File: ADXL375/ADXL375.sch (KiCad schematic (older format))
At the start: 23 parts, among them J1 Conn_01x06, J2 Conn_01x04, J3 Conn_01x06, J4 Conn_01x04, Q1 BSS138DW, Q2 BSS138DW, U1 AP2127K-3.3, U2 ADXL345

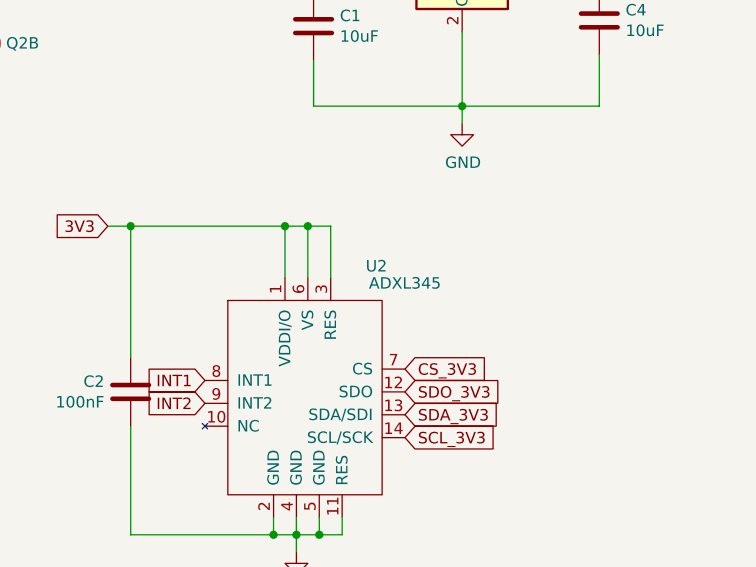
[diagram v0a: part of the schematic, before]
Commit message: ADXL375 Schematic Update
ADXL345 changed to ADXL375
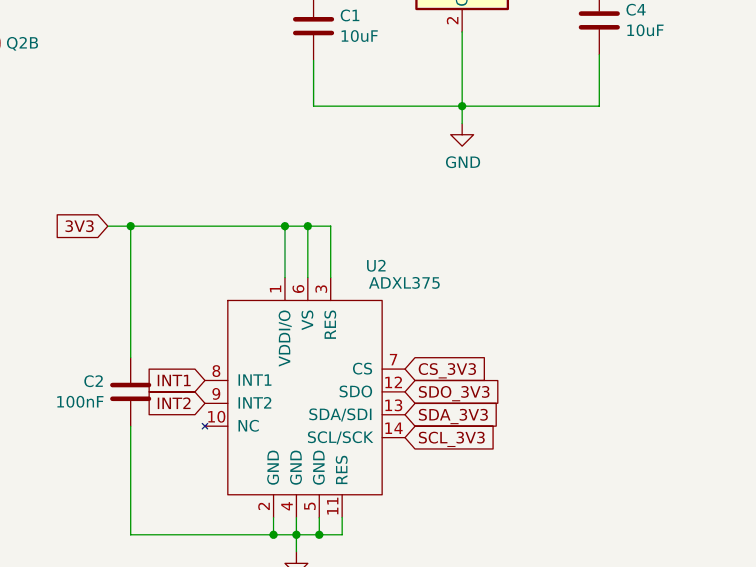
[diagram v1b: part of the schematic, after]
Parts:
- U2: value ADXL345 -> ADXL375; Part C9667 -> C481898
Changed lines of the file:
@@
 P 5375 3200
 F 0 "U2" H 5675 3800 50  0000 C CNN
-F 1 "ADXL345" H 5800 3725 50  0000 C CNN
+F 1 "ADXL375" H 5800 3725 50  0000 C CNN
 F 2 "Package_LGA:LGA-14_3x5mm_P0.8mm_LayoutBorder1x6y" H 5375 3775 50  0001 C CNN
-F 3 "" H 5375 3775 50  0001 C CNN
-F 4 "C9667" H 5362 3838 50  0001 C CNN "Part"
+F 3 "https://docs.rs-online.com/c088/0900766b812d72c4.pdf" H 5375 3775 50  0001 C CNN
+F 4 "C481898" H 5362 3838 50  0001 C CNN "Part"
 	1    5375 3200
 	1    0    0    -1
